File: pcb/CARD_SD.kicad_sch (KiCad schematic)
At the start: 6 parts, among them J5 GSD09002SEU

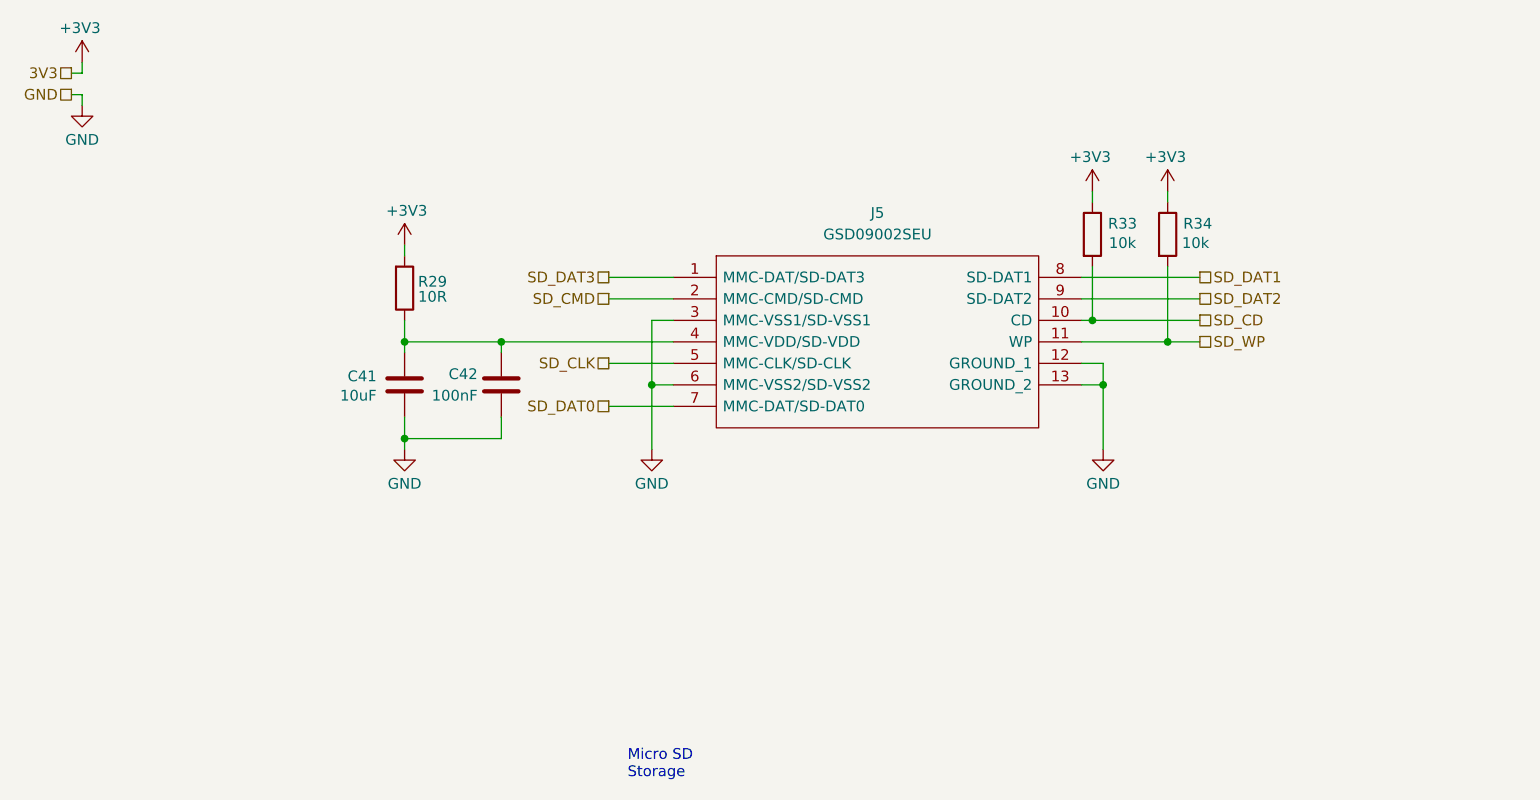
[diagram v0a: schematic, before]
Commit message: updated pcie sd and sim cards
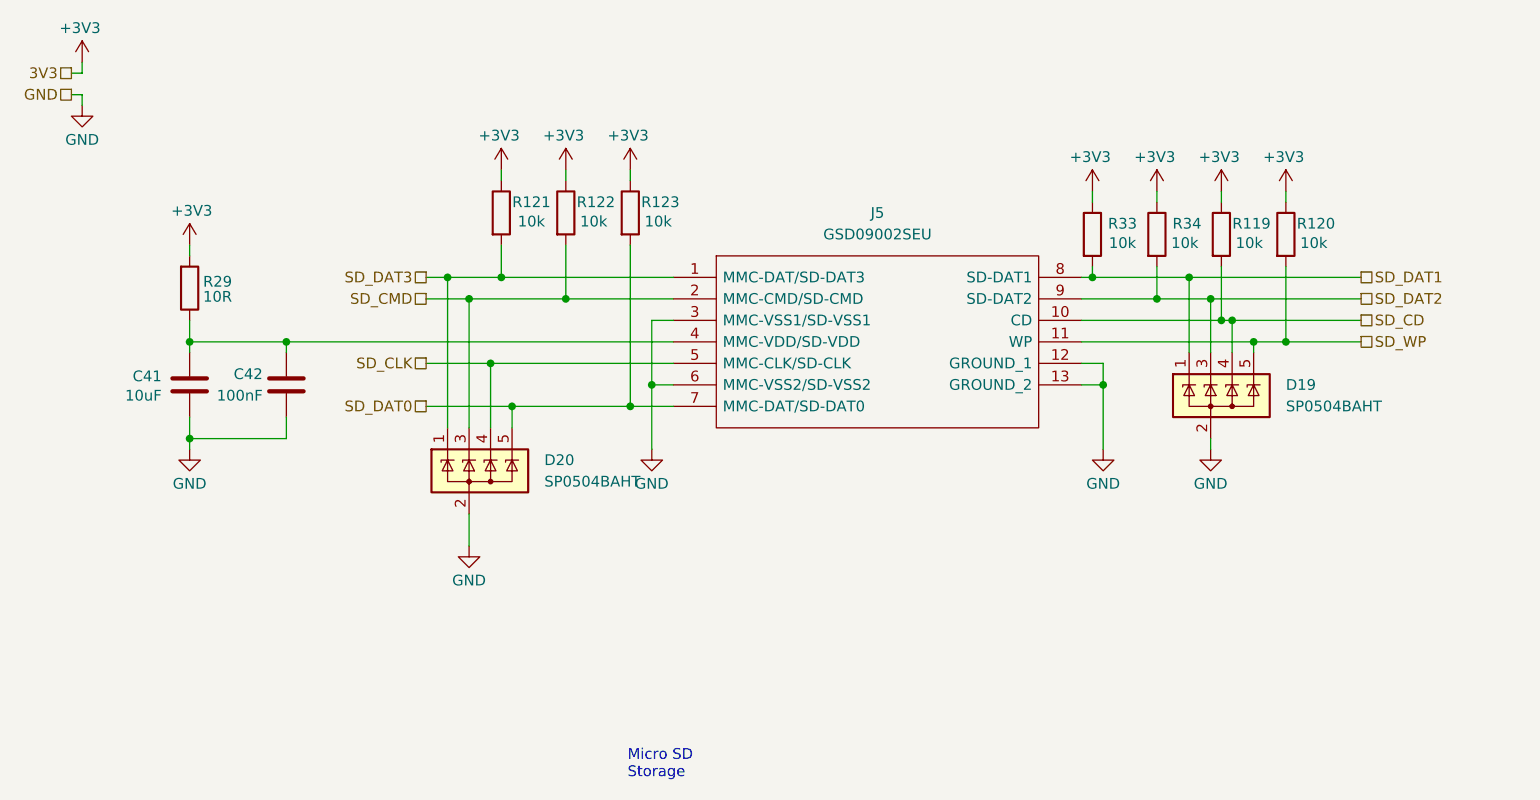
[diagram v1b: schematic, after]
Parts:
- added D19, D20: SP0504BAHT, Package_TO_SOT_SMD:SOT-23-5, symbol Power_Protection:SP0504BAHT
- added R119, R120, R121, R122, R123: 10k, Resistor_SMD:R_0603_1608Metric_Pad0.98x0.95mm_HandSolder, symbol Device:R
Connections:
- net +3V3: now also R119.1, R120.1, R121.1, R122.1, R123.1
- net GND: now also D19.2 (A), D20.2 (A)
- net SD_CD: now also D19.4 (K), R119.2; no longer R33.2
- net SD_CLK: now also D20.4 (K)
- net SD_CMD: now also D20.3 (K), R122.2
- net SD_DAT0: now also D20.5 (K), R123.2
- net SD_DAT1: now also R33.2, D19.1 (K)
- net SD_DAT2: now also R34.2, D19.3 (K)
- net SD_DAT3: now also D20.1 (K), R121.2
- net SD_WP: now also D19.5 (K), R120.2; no longer R34.2
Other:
- moved on the sheet: C41, C42, R29, R34

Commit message: reannotated, updated some symbols
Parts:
- renumbered C41 to C46, C42 to C47, D20 to D10, D19 to D12, R29 to R36, R121 to R37, R122 to R38, R123 to R41, R33 to R43, R34 to R44, R119 to R45, R120 to R46
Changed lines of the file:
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@@
 		(on_board yes)
 		(dnp no)
-		(property "Reference" "R34"
+		(property "Reference" "R44"
 			(at 157.226 43.18 0)
 			(effects
@@
 			(project "NCU"
 				(path "/3aee14c3-5480-4f7c-989e-3fef81779034/59880cb1-7ec0-4ddb-9063-a30a9ec86eac"
-					(reference "R34")
+					(reference "R44")
 					(unit 1)
 				)
@@
 		(on_board yes)
 		(dnp no)
-		(property "Reference" "#PWR0186"
+		(property "Reference" "#PWR0231"
 			(at 39.37 76.2 0)
 			(effects
@@
 			(project "NCU"
 				(path "/3aee14c3-5480-4f7c-989e-3fef81779034/59880cb1-7ec0-4ddb-9063-a30a9ec86eac"
-					(reference "#PWR0186")
+					(reference "#PWR0231")
 					(unit 1)
 				)
@@
 		(on_board yes)
 		(dnp no)
-		(property "Reference" "#PWR0421"
+		(property "Reference" "#PWR0234"
 			(at 83.82 40.64 0)
 			(effects
@@
 			(project "NCU"
 				(path "/3aee14c3-5480-4f7c-989e-3fef81779034/59880cb1-7ec0-4ddb-9063-a30a9ec86eac"
-					(reference "#PWR0421")
+					(reference "#PWR0234")
 					(unit 1)
 				)
@@
 		(on_board yes)
 		(dnp no)
-		(property "Reference" "#PWR0419"
+		(property "Reference" "#PWR0232"
 			(at 72.39 87.63 0)
 			(effects
@@
 			(project "NCU"
 				(path "/3aee14c3-5480-4f7c-989e-3fef81779034/59880cb1-7ec0-4ddb-9063-a30a9ec86eac"
-					(reference "#PWR0419")
+					(reference "#PWR0232")
 					(unit 1)
 				)
@@
 		(on_board yes)
 		(dnp no)
-		(property "Reference" "#PWR0192"
+		(property "Reference" "#PWR0243"
 			(at 153.67 43.18 0)
 			(effects
@@
 			(project "NCU"
 				(path "/3aee14c3-5480-4f7c-989e-3fef81779034/59880cb1-7ec0-4ddb-9063-a30a9ec86eac"
-					(reference "#PWR0192")
+					(reference "#PWR0243")
 					(unit 1)
 				)
@@
 		(on_board yes)
 		(dnp no)
-		(property "Reference" "#PWR0190"
+		(property "Reference" "#PWR0241"
 			(at 146.05 43.18 0)
 			(effects
@@
 			(project "NCU"
 				(path "/3aee14c3-5480-4f7c-989e-3fef81779034/59880cb1-7ec0-4ddb-9063-a30a9ec86eac"
-					(reference "#PWR0190")
+					(reference "#PWR0241")
 					(unit 1)
 				)
@@
 		(on_board yes)
 		(dnp no)
-		(property "Reference" "#PWR0191"
+		(property "Reference" "#PWR0242"
 			(at 147.32 76.2 0)
 			(effects
@@
 			(project "NCU"
 				(path "/3aee14c3-5480-4f7c-989e-3fef81779034/59880cb1-7ec0-4ddb-9063-a30a9ec86eac"
-					(reference "#PWR0191")
+					(reference "#PWR0242")
 					(unit 1)
 				)
@@
 		(on_board yes)
 		(dnp no)
-		(property "Reference" "R123"
+		(property "Reference" "R41"
 			(at 94.996 40.64 0)
 			(effects
@@
 			(project "NCU"
 				(path "/3aee14c3-5480-4f7c-989e-3fef81779034/59880cb1-7ec0-4ddb-9063-a30a9ec86eac"
-					(reference "R123")
+					(reference "R41")
 					(unit 1)
 				)
@@
 		(on_board yes)
 		(dnp no)
-		(property "Reference" "#PWR0182"
+		(property "Reference" "#PWR0226"
 			(at 26.67 27.94 0)
 			(effects
@@
 			(project "NCU"
 				(path "/3aee14c3-5480-4f7c-989e-3fef81779034/59880cb1-7ec0-4ddb-9063-a30a9ec86eac"
-					(reference "#PWR0182")
+					(reference "#PWR0226")
 					(unit 1)
 				)
@@
 		(on_board yes)
 		(dnp no)
-		(property "Reference" "R29"
+		(property "Reference" "R36"
 			(at 42.672 50.038 0)
 			(effects
@@
 			(project "NCU"
 				(path "/3aee14c3-5480-4f7c-989e-3fef81779034/59880cb1-7ec0-4ddb-9063-a30a9ec86eac"
-					(reference "R29")
+					(reference "R36")
 					(unit 1)
 				)
@@
 		(on_board yes)
 		(dnp no)
-		(property "Reference" "#PWR0417"
+		(property "Reference" "#PWR0246"
 			(at 168.91 43.18 0)
 			(effects
@@
 			(project "NCU"
 				(path "/3aee14c3-5480-4f7c-989e-3fef81779034/59880cb1-7ec0-4ddb-9063-a30a9ec86eac"
-					(reference "#PWR0417")
+					(reference "#PWR0246")
 					(unit 1)
 				)
@@
 		(on_board yes)
 		(dnp no)
-		(property "Reference" "#PWR0418"
+		(property "Reference" "#PWR0244"
 			(at 160.02 76.2 0)
 			(effects
@@
 			(project "NCU"
 				(path "/3aee14c3-5480-4f7c-989e-3fef81779034/59880cb1-7ec0-4ddb-9063-a30a9ec86eac"
-					(reference "#PWR0418")
+					(reference "#PWR0244")
 					(unit 1)
 				)
@@
 		(dnp no)
 		(fields_autoplaced yes)
-		(property "Reference" "D19"
+		(property "Reference" "D12"
 			(at 168.91 62.2299 0)
 			(effects
@@
 			(project ""
 				(path "/3aee14c3-5480-4f7c-989e-3fef81779034/59880cb1-7ec0-4ddb-9063-a30a9ec86eac"
-					(reference "D19")
+					(reference "D12")
 					(unit 1)
 				)
@@
 		(dnp no)
 		(fields_autoplaced yes)
-		(property "Reference" "D20"
+		(property "Reference" "D10"
 			(at 81.28 71.1199 0)
 			(effects
@@
 			(project "NCU"
 				(path "/3aee14c3-5480-4f7c-989e-3fef81779034/59880cb1-7ec0-4ddb-9063-a30a9ec86eac"
-					(reference "D20")
+					(reference "D10")
 					(unit 1)
 				)
@@
 		(on_board yes)
 		(dnp no)
-		(property "Reference" "#PWR0420"
+		(property "Reference" "#PWR0233"
 			(at 76.2 40.64 0)
 			(effects
@@
 			(project "NCU"
 				(path "/3aee14c3-5480-4f7c-989e-3fef81779034/59880cb1-7ec0-4ddb-9063-a30a9ec86eac"
-					(reference "#PWR0420")
+					(reference "#PWR0233")
 					(unit 1)
 				)
@@
 		(on_board yes)
 		(dnp no)
-		(property "Reference" "#PWR0183"
+		(property "Reference" "#PWR0227"
 			(at 26.67 35.56 0)
 			(effects
@@
 			(project "NCU"
 				(path "/3aee14c3-5480-4f7c-989e-3fef81779034/59880cb1-7ec0-4ddb-9063-a30a9ec86eac"
-					(reference "#PWR0183")
+					(reference "#PWR0227")
 					(unit 1)
 				)
@@
 		(on_board yes)
 		(dnp no)
-		(property "Reference" "#PWR0422"
+		(property "Reference" "#PWR0236"
 			(at 91.44 40.64 0)
 			(effects
@@
 			(project "NCU"
 				(path "/3aee14c3-5480-4f7c-989e-3fef81779034/59880cb1-7ec0-4ddb-9063-a30a9ec86eac"
-					(reference "#PWR0422")
+					(reference "#PWR0236")
 					(unit 1)
 				)
@@
 		(on_board yes)
 		(dnp no)
-		(property "Reference" "R122"
+		(property "Reference" "R38"
 			(at 87.376 40.64 0)
 			(effects
@@
 			(project "NCU"
 				(path "/3aee14c3-5480-4f7c-989e-3fef81779034/59880cb1-7ec0-4ddb-9063-a30a9ec86eac"
-					(reference "R122")
+					(reference "R38")
 					(unit 1)
 				)
@@
 		(on_board yes)
 		(dnp no)
-		(property "Reference" "#PWR0188"
+		(property "Reference" "#PWR0237"
 			(at 93.98 76.2 0)
 			(effects
@@
 			(project "NCU"
 				(path "/3aee14c3-5480-4f7c-989e-3fef81779034/59880cb1-7ec0-4ddb-9063-a30a9ec86eac"
-					(reference "#PWR0188")
+					(reference "#PWR0237")
 					(unit 1)
 				)
@@
 		(on_board yes)
 		(dnp no)
-		(property "Reference" "#PWR0416"
+		(property "Reference" "#PWR0245"
 			(at 161.29 43.18 0)
 			(effects
@@
 			(project "NCU"
 				(path "/3aee14c3-5480-4f7c-989e-3fef81779034/59880cb1-7ec0-4ddb-9063-a30a9ec86eac"
-					(reference "#PWR0416")
+					(reference "#PWR0245")
 					(unit 1)
 				)
@@
 		(on_board yes)
 		(dnp no)
-		(property "Reference" "R120"
+		(property "Reference" "R46"
 			(at 172.466 43.18 0)
 			(effects
@@
 			(project "NCU"
 				(path "/3aee14c3-5480-4f7c-989e-3fef81779034/59880cb1-7ec0-4ddb-9063-a30a9ec86eac"
-					(reference "R120")
+					(reference "R46")
 					(unit 1)
 				)
@@
 		(on_board yes)
 		(dnp no)
-		(property "Reference" "C41"
+		(property "Reference" "C46"
 			(at 36.068 61.214 0)
 			(effects
@@
 			(project "NCU"
 				(path "/3aee14c3-5480-4f7c-989e-3fef81779034/59880cb1-7ec0-4ddb-9063-a30a9ec86eac"
-					(reference "C41")
+					(reference "C46")
 					(unit 1)
 				)
@@
 		(on_board yes)
 		(dnp no)
-		(property "Reference" "#PWR0185"
+		(property "Reference" "#PWR0230"
 			(at 39.37 49.53 0)
 			(effects
@@
 			(project "NCU"
 				(path "/3aee14c3-5480-4f7c-989e-3fef81779034/59880cb1-7ec0-4ddb-9063-a30a9ec86eac"
-					(reference "#PWR0185")
+					(reference "#PWR0230")
 					(unit 1)
 				)
@@
 		(on_board yes)
 		(dnp no)
-		(property "Reference" "C42"
+		(property "Reference" "C47"
 			(at 48.006 60.96 0)
 			(effects
@@
 			(project "NCU"
 				(path "/3aee14c3-5480-4f7c-989e-3fef81779034/59880cb1-7ec0-4ddb-9063-a30a9ec86eac"
-					(reference "C42")
+					(reference "C47")
 					(unit 1)
 				)
@@
 		(on_board yes)
 		(dnp no)
-		(property "Reference" "R33"
+		(property "Reference" "R43"
 			(at 149.606 43.18 0)
 			(effects
@@
 			(project "NCU"
 				(path "/3aee14c3-5480-4f7c-989e-3fef81779034/59880cb1-7ec0-4ddb-9063-a30a9ec86eac"
-					(reference "R33")
+					(reference "R43")
 					(unit 1)
 				)
@@
 		(on_board yes)
 		(dnp no)
-		(property "Reference" "R121"
+		(property "Reference" "R37"
 			(at 79.756 40.64 0)
 			(effects
@@
 			(project "NCU"
 				(path "/3aee14c3-5480-4f7c-989e-3fef81779034/59880cb1-7ec0-4ddb-9063-a30a9ec86eac"
-					(reference "R121")
+					(reference "R37")
 					(unit 1)
 				)
@@
 		(on_board yes)
 		(dnp no)
-		(property "Reference" "R119"
+		(property "Reference" "R45"
 			(at 164.846 43.18 0)
 			(effects
@@
 			(project "NCU"
 				(path "/3aee14c3-5480-4f7c-989e-3fef81779034/59880cb1-7ec0-4ddb-9063-a30a9ec86eac"
-					(reference "R119")
-					(unit 1)
-				)
+					(reference "R45")
+					(unit 1)
+				)

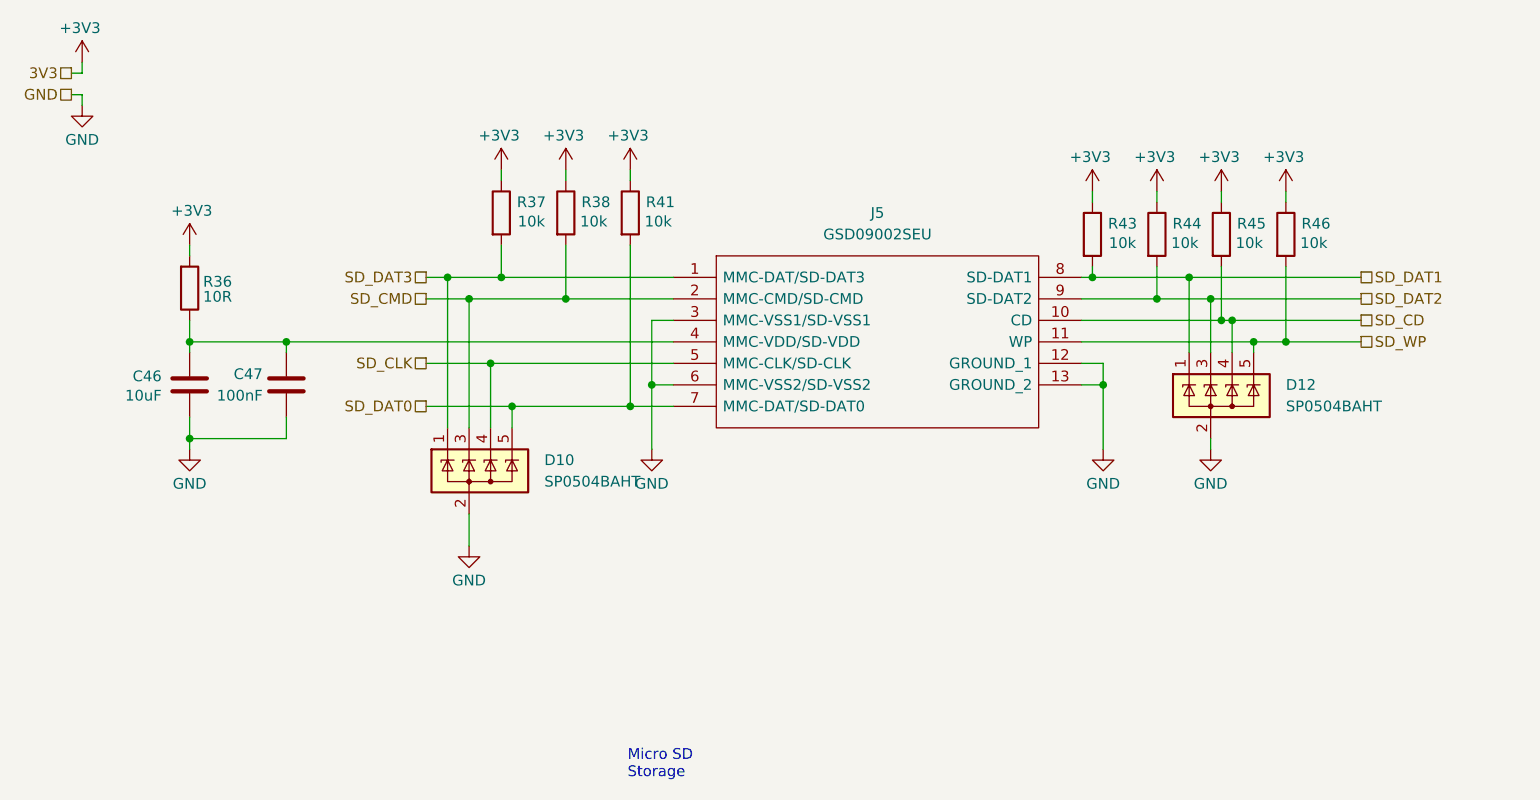
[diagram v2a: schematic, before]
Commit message: swapped sd to micro sd
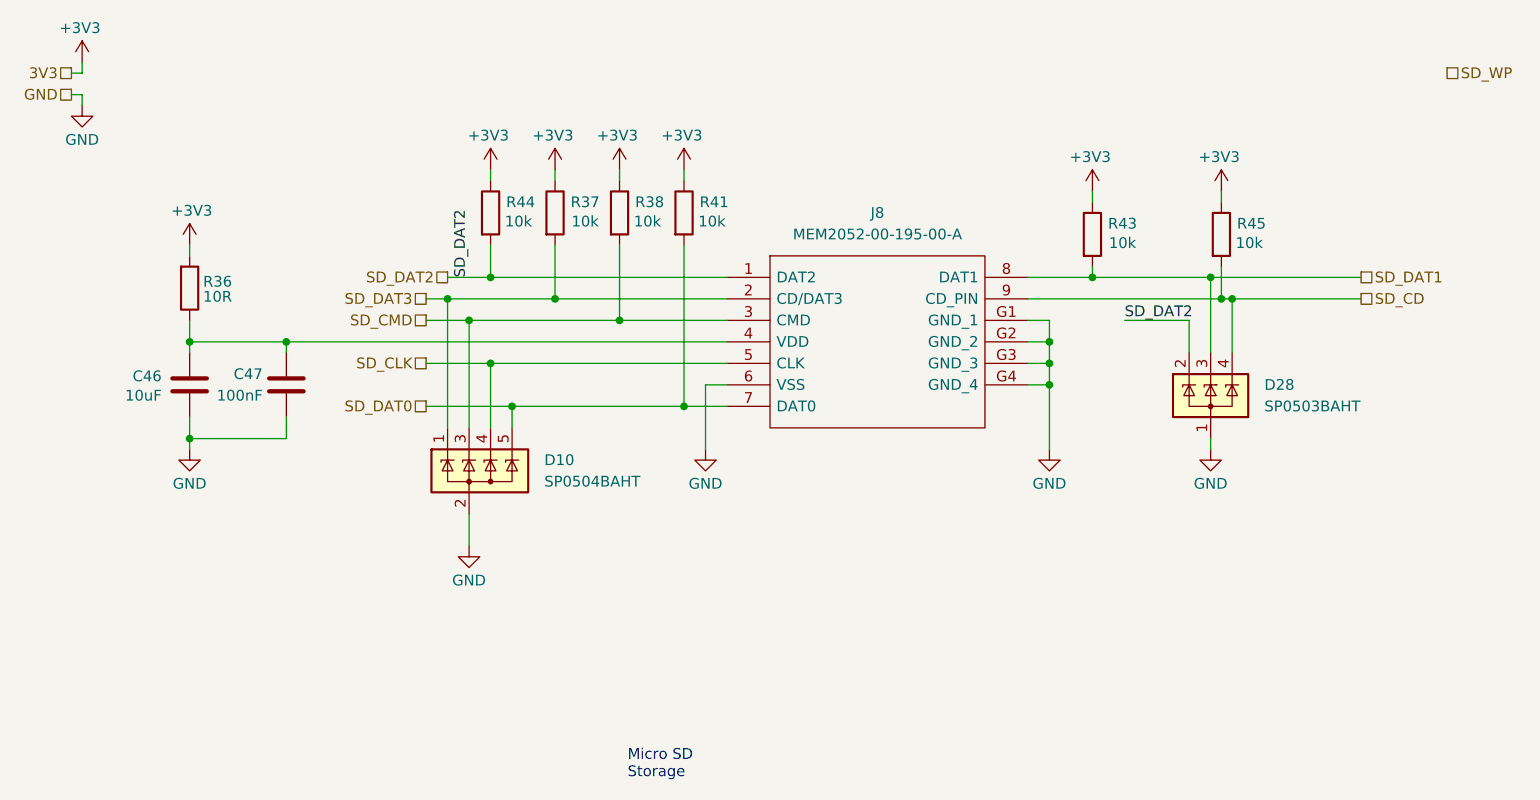
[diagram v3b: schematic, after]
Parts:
- removed D12: SP0504BAHT, Package_TO_SOT_SMD:SOT-23-5, symbol Power_Protection:SP0504BAHT
- removed J5: GSD09002SEU, GSD09002SEU, symbol 0_SamacSys_Parts:GSD09002SEU
- removed R46: 10k, Resistor_SMD:R_0603_1608Metric_Pad0.98x0.95mm_HandSolder, symbol Device:R
- added D28: SP0503BAHT, Package_TO_SOT_SMD:SOT-143, symbol Power_Protection:SP0503BAHT
- added J8: MEM2052-00-195-00-A, MEM20520019500A, symbol 0_SamacSys_Parts:MEM2052-00-195-00-A
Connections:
- net GND: now also D28.1 (A), J8.6 (VSS), J8.G1 (GND_1), J8.G2 (GND_2), J8.G3 (GND_3), J8.G4 (GND_4)
- net SD_CD: now also D28.4 (K), J8.9 (CD_PIN)
- net SD_CLK: now also J8.5 (CLK)
- net SD_CMD: now also J8.3 (CMD)
- net SD_DAT0: now also J8.7 (DAT0)
- net SD_DAT1: now also D28.3 (K), J8.8 (DAT1)
- net SD_DAT2: now also D28.2 (K), J8.1 (DAT2)
- net SD_DAT3: now also J8.2 (CD/DAT3)
- net at C46.1, C47.1, R36.1: now also J8.4 (VDD)
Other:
- moved on the sheet: R37, R38, R41, R44

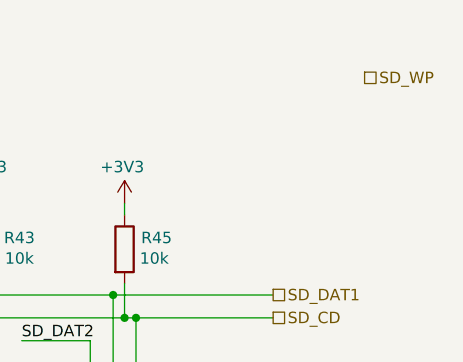
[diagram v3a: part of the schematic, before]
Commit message: sd card slot initial attempt (I meant SIM before)
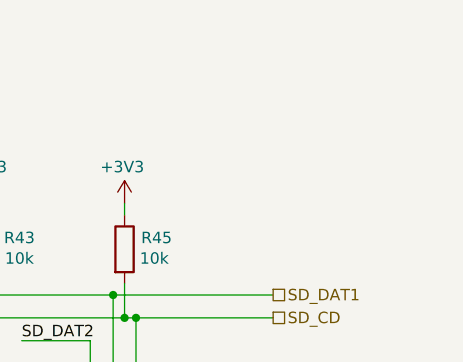
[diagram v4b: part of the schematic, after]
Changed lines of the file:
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@@
-		)
-	)
-	(hierarchical_label "SD_WP"
-		(shape passive)
-		(at 187.96 25.4 0)
-		(effects
-			(font
-				(size 1.27 1.27)
-			)
-			(justify left)
 		)
 	)
